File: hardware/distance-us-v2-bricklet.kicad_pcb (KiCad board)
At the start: 2 copper layers, 30 x 30 mm, 26 parts, among them P1 CON-SENSOR2, P2 DEBUG, P3 BOOT, U1 XMC1XXX24, U2 DRILL, U3 DRILL, U4 DRILL, U5 DRILL, U6 HRLV-EZ

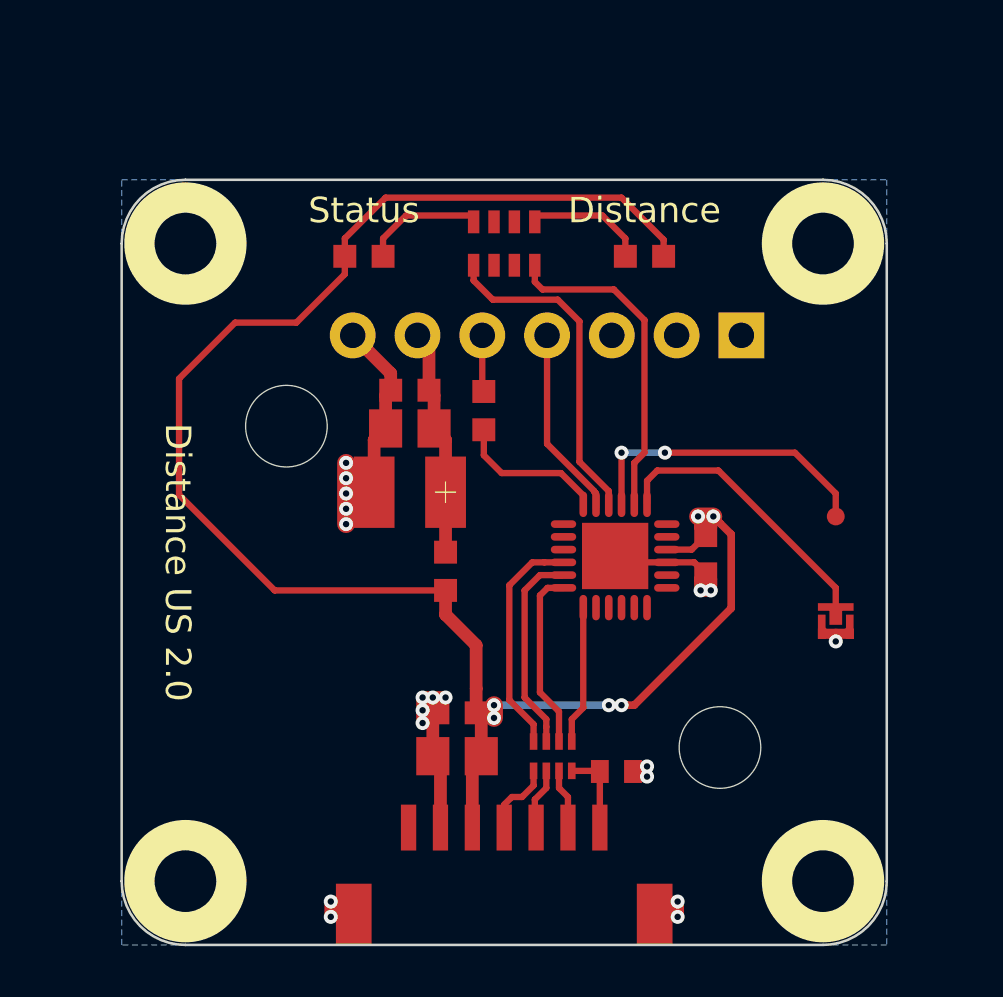
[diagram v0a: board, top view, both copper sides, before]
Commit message: changed sensor footprint, new pcb design
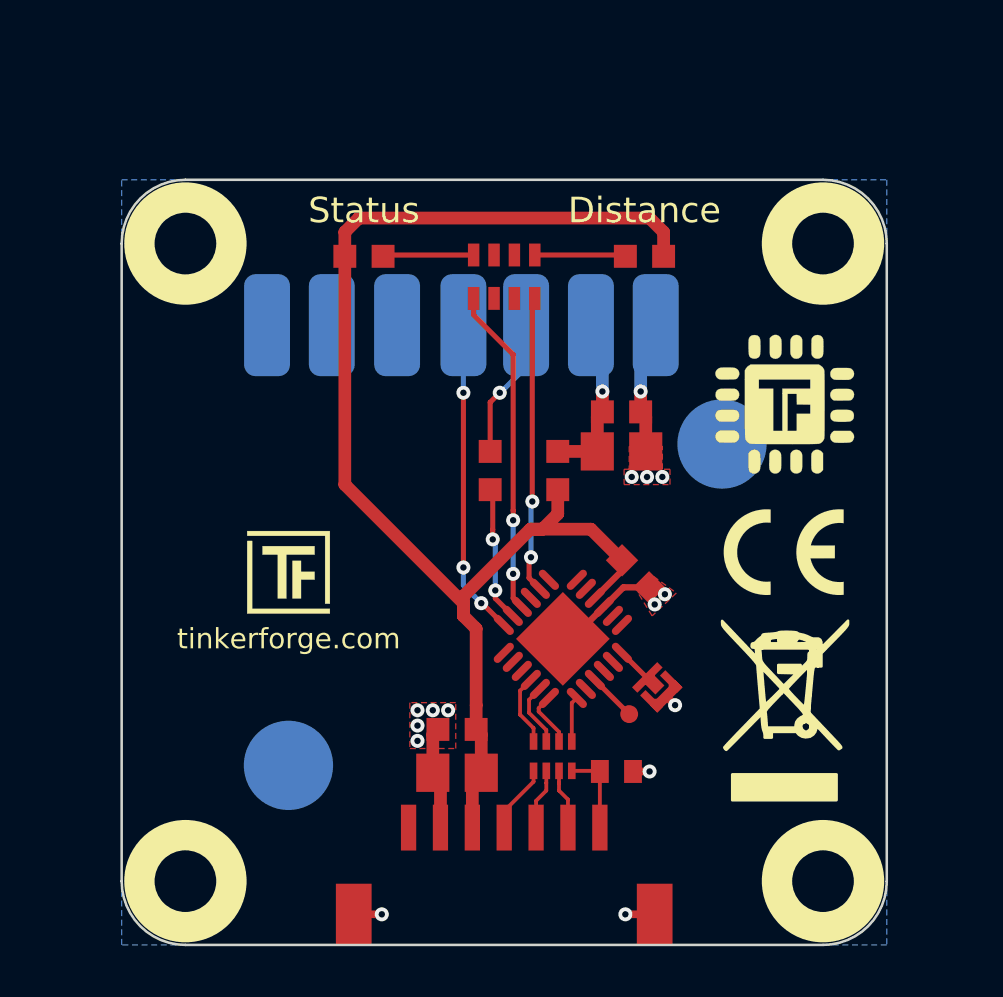
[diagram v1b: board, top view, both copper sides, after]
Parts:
- removed C5: 100uF, 3528-21
- G***, VAL (x2): moved to F.Cu
- G***: value Logo_31x31 -> LOGO; moved to F.Cu
- U1: value XMC1XXX24 -> XMC1100
- U6: footprint kicad-libraries:HRLV-EZ -> kicad-libraries:HRLV-EZ(SMD_EX); moved to B.Cu
- moved VAL 19.7 mm to (161.0, 108.3), turned to 0 degrees
- moved G*** 13.8 mm to (161.0, 96.3), turned to 0 degrees
- moved G*** 12.4 mm to (141.6, 102.9), turned to 0 degrees
- moved P2 11.2 mm to (154.9, 108.5)
- moved C6 8.35 mm to (154.6, 98.2), turned to 0 degrees
- moved C7 8.34 mm to (154.6, 96.6), turned to 0 degrees
- moved P3 7.47 mm to (156.0, 107.4), turned to 135 degrees
- moved L1 5.91 mm to (152.1, 98.9)
- moved U1 3.84 mm to (152.3, 105.5), turned to 135 degrees
- moved VAL 3.54 mm to (161.0, 102.1), turned to 0 degrees
- moved C4 2.85 mm to (155.2, 103.0), turned to 315 degrees
- moved R1 2.36 mm to (149.4, 98.9)
- moved RP2 1.30 mm to (150.0, 91.3)
- moved U6 0.70 mm to (150.0, 103.2), turned to 180 degrees
- moved C2 0.65 mm to (148.2, 110.8)
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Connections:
- U1 pad 13: Net-(P3-Pad2) -> Net-(U1-Pad13)
- U1 pad 15: Net-(P2-Pad1) -> Net-(U1-Pad15)
- U1 pad 17: Ranging -> Serial
- U1 pad 18: Serial -> Ranging
- U1 pad 3: Net-(U1-Pad3) -> Net-(P2-Pad1)
- U1 pad 6: Net-(U1-Pad6) -> Net-(P3-Pad2)
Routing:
- net 3V3: track 72.6 -> 52.4 mm, vias 6 -> 0
- net GND: track 35.0 -> 21.6 mm, vias 19 -> 15
- net Net-(P2-Pad1): track 12.0 -> 1.77 mm, vias 2 -> 0
- net Net-(P3-Pad2): track 11.3 -> 1.79 mm
- net S-CS: track 9.02 -> 2.81 mm
- net S-CLK: track 8.05 -> 2.52 mm
- net S-MOSI: track 7.08 -> 2.21 mm
- net Ranging: track 7.60 -> 12.4 mm, vias 0 -> 3
- net S-MISO: track 5.44 -> 1.79 mm
- net Net-(R1-Pad1): track 2.22 -> 5.61 mm, vias 0 -> 1
- net Net-(C6-Pad1): track 8.96 -> 6.77 mm, vias 0 -> 1
- net Net-(RP2-Pad5): track 13.1 -> 11.7 mm, vias 0 -> 2
- net Net-(D2-Pad2): track 4.62 -> 3.57 mm
- net Net-(D1-Pad2): track 4.62 -> 3.57 mm
- net Net-(P1-Pad6): track 1.47 -> 2.37 mm
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- added copper zone on F.Cu, net GND

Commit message: drc check, plotted 2 differnt footprints of HRLV for prototyp
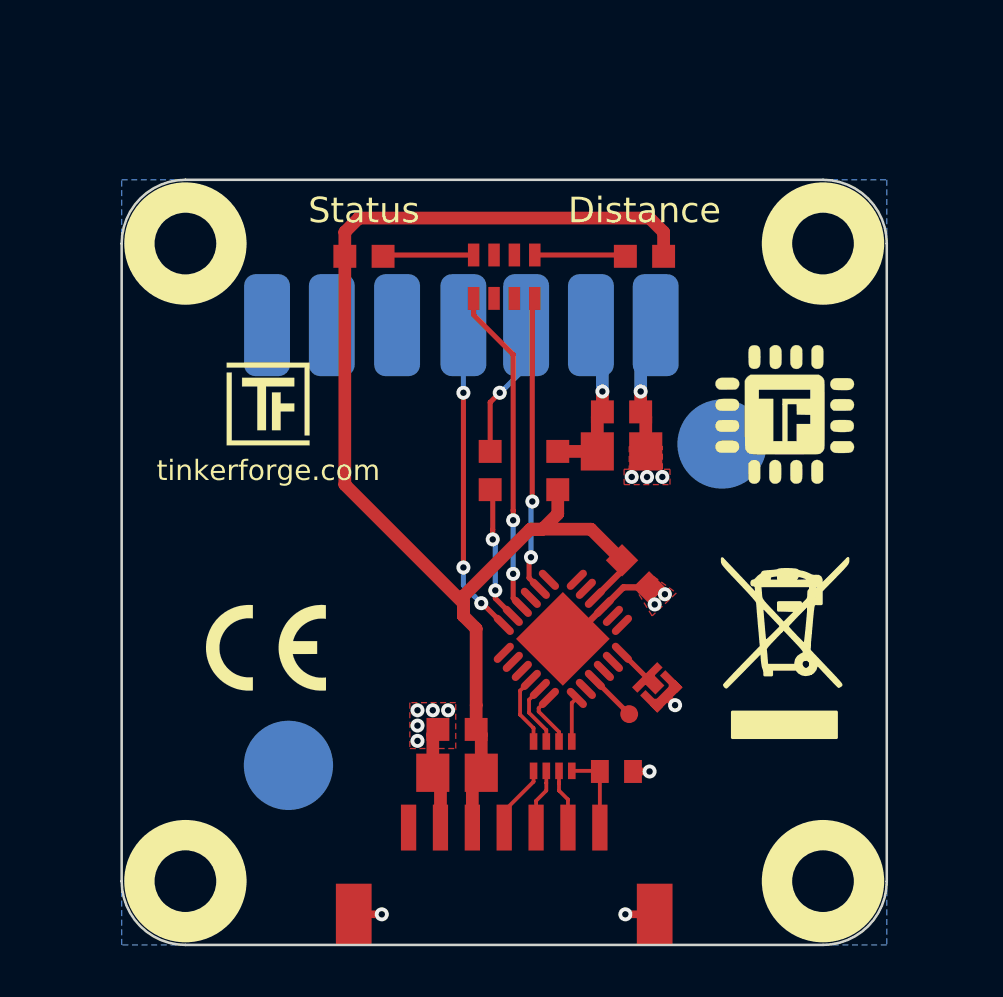
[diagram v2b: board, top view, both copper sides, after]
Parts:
- moved VAL 20.6 mm to (140.7, 105.8)
- moved G*** 6.65 mm to (140.8, 96.3)
- moved VAL 2.45 mm to (161.0, 105.8)
- moved G*** 0.40 mm to (161.0, 96.7)

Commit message: new 35x35 design
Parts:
- added G***: LOGO, kicad-libraries:Logo_31x31, B.Cu at (150.0, 84.8)
- moved U4 5.59 mm to (135.0, 85.0)
- moved U5 5.59 mm to (165.0, 85.0)
- moved D1 5.00 mm to (144.5, 85.5)
- moved D2 5.00 mm to (155.5, 85.5)
- moved RP2 5.00 mm to (150.0, 86.3)
- moved G*** 4.40 mm to (138.2, 92.8)
- moved G*** 3.89 mm to (163.3, 93.6)
- moved C6 3.00 mm to (154.6, 95.2)
- moved C7 3.00 mm to (154.6, 93.6)
- moved U6 3.00 mm to (150.0, 100.2)
- moved L1 2.95 mm to (152.1, 96.0)
- moved R1 2.95 mm to (149.4, 96.0)
- moved VAL 2.60 mm to (138.1, 105.8)
- moved U2 2.50 mm to (165.0, 115.0)
- moved U3 2.50 mm to (135.0, 115.0)
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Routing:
- net 3V3: track 52.4 -> 90.4 mm
- net Net-(RP2-Pad5): track 11.7 -> 16.7 mm, vias 2 -> 0
- net Net-(RP2-Pad8): track 12.9 -> 17.9 mm, vias 2 -> 0
- net Serial: track 5.38 -> 8.27 mm, vias 2 -> 0
- net Ranging: track 12.4 -> 15.2 mm, vias 3 -> 1
- net GND: track 21.6 -> 22.2 mm
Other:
- board size 30 x 30 mm -> 35 x 35 mm
- net class Default: clearance 0.15 -> 0.149
- rule trace_clearance: 0.15 -> 0.149

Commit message: changed HRLV footprint and centered it
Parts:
- moved G*** 27.7 mm to (150.0, 112.5)
- moved U6 0.20 mm to (150.0, 100.0)

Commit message: add fiducials, drc
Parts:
- added Fiducial_Mark: VAL**, kicad-libraries:Fiducial_Mark, F.Cu at (140.5, 112.5)
- added Fiducial_Mark: VAL**, kicad-libraries:Fiducial_Mark, F.Cu at (159.5, 114.5)
- added Fiducial_Mark: VAL**, kicad-libraries:Fiducial_Mark, F.Cu at (135.5, 90.5)
- added Fiducial_Mark: VAL**, kicad-libraries:Fiducial_Mark, F.Cu at (159.5, 98.5)
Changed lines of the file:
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@@
-(kicad_pcb (version 20171130) (host pcbnew 5.0.2-bee76a0~70~ubuntu18.10.1)
+(kicad_pcb (version 20171130) (host pcbnew 5.0.2-bee76a0~70~ubuntu18.04.1)
   (general
     (thickness 1.6)
@@
     (tracks 143)
     (zones 0)
-    (modules 26)
+    (modules 30)
     (nets 41)
   )
@@
       (xy -1.62681 1.239762) (xy -1.433286 1.239762) (xy -1.433286 -1.42119)) (layer B.SilkS) (width 0.01))
   )
+  (module kicad-libraries:Fiducial_Mark (layer F.Cu)
+    (at 140.5 112.5)
+    (attr smd)
+    (fp_text reference Fiducial_Mark (at 0 0) (layer F.SilkS) hide
+      (effects (font (size 0.127 0.127) (thickness 0.03302)))
+    )
+    (fp_text value VAL** (at 0 -0.29972) (layer F.SilkS) hide
+      (effects (font (size 0.127 0.127) (thickness 0.03302)))
+    )
+    (fp_circle (center 0 0) (end 1.15062 0) (layer Dwgs.User) (width 0.01016))
+    (pad 1 smd circle (at 0 0) (size 1.00076 1.00076) (layers F.Cu F.Paste F.Mask)
+      (clearance 0.65024))
+  )
+  (module kicad-libraries:Fiducial_Mark (layer F.Cu)
+    (at 159.5 114.5)
+    (attr smd)
+    (fp_text reference Fiducial_Mark (at 0 0) (layer F.SilkS) hide
+      (effects (font (size 0.127 0.127) (thickness 0.03302)))
+    )
+    (fp_text value VAL** (at 0 -0.29972) (layer F.SilkS) hide
+      (effects (font (size 0.127 0.127) (thickness 0.03302)))
+    )
+    (fp_circle (center 0 0) (end 1.15062 0) (layer Dwgs.User) (width 0.01016))
+    (pad 1 smd circle (at 0 0) (size 1.00076 1.00076) (layers F.Cu F.Paste F.Mask)
+      (clearance 0.65024))
+  )
+  (module kicad-libraries:Fiducial_Mark (layer F.Cu)
+    (at 135.5 90.5)
+    (attr smd)
+    (fp_text reference Fiducial_Mark (at 0 0) (layer F.SilkS) hide
+      (effects (font (size 0.127 0.127) (thickness 0.03302)))
+    )
+    (fp_text value VAL** (at 0 -0.29972) (layer F.SilkS) hide
+      (effects (font (size 0.127 0.127) (thickness 0.03302)))
+    )
+    (fp_circle (center 0 0) (end 1.15062 0) (layer Dwgs.User) (width 0.01016))
+    (pad 1 smd circle (at 0 0) (size 1.00076 1.00076) (layers F.Cu F.Paste F.Mask)
+      (clearance 0.65024))
+  )
+  (module kicad-libraries:Fiducial_Mark (layer F.Cu)
+    (at 159.5 98.5)
+    (attr smd)
+    (fp_text reference Fiducial_Mark (at 0 0) (layer F.SilkS) hide
+      (effects (font (size 0.127 0.127) (thickness 0.03302)))
+    )
+    (fp_text value VAL** (at 0 -0.29972) (layer F.SilkS) hide
+      (effects (font (size 0.127 0.127) (thickness 0.03302)))
+    )
+    (fp_circle (center 0 0) (end 1.15062 0) (layer Dwgs.User) (width 0.01016))
+    (pad 1 smd circle (at 0 0) (size 1.00076 1.00076) (layers F.Cu F.Paste F.Mask)
+      (clearance 0.65024))
+  )
   (gr_text tinkerforge.com (at 150 115) (layer B.SilkS)
